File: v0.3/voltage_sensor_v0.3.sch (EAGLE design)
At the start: 56 parts, among them IC1 AP2112K-3.3TRG1, J2 236-404_000-009_999-950, J3 MC000048, J9 RJ11, T1 ZMPT101B, T2 ZMPT101B, T3 ZMPT101B

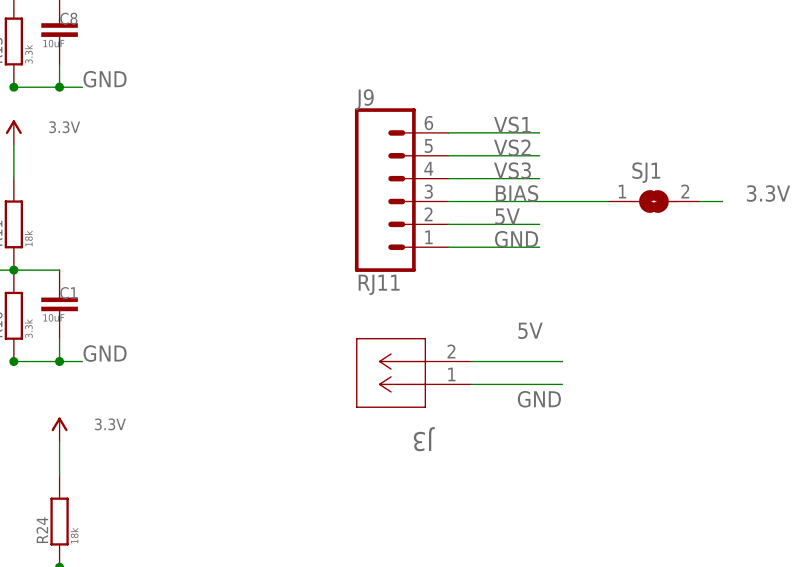
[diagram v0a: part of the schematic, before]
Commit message: rename change log
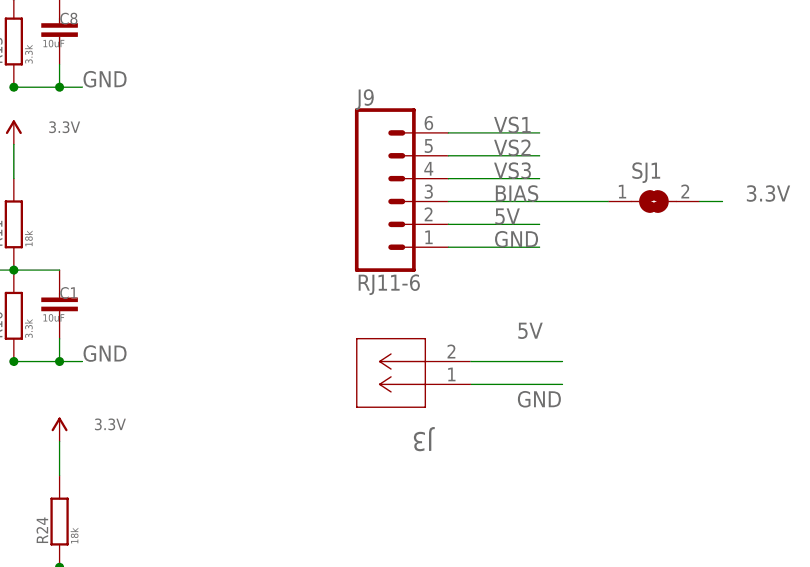
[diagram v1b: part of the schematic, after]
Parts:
- J9: value RJ11 -> RJ11-6
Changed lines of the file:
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@@
 <parts>
 <part name="T1" library="ZMPT101B" deviceset="ZMPT101B" device=""/>
-<part name="J9" library="SparkFun-Connectors" deviceset="RJ11-6" device="" value="RJ11"/>
+<part name="J9" library="SparkFun-Connectors" deviceset="RJ11-6" device="" value="RJ11-6"/>
 <part name="R22" library="rcl" deviceset="R-EU_" device="0204/7"/>
 <part name="R9" library="rcl" deviceset="R-EU_" device="R0603" value="75R"/>

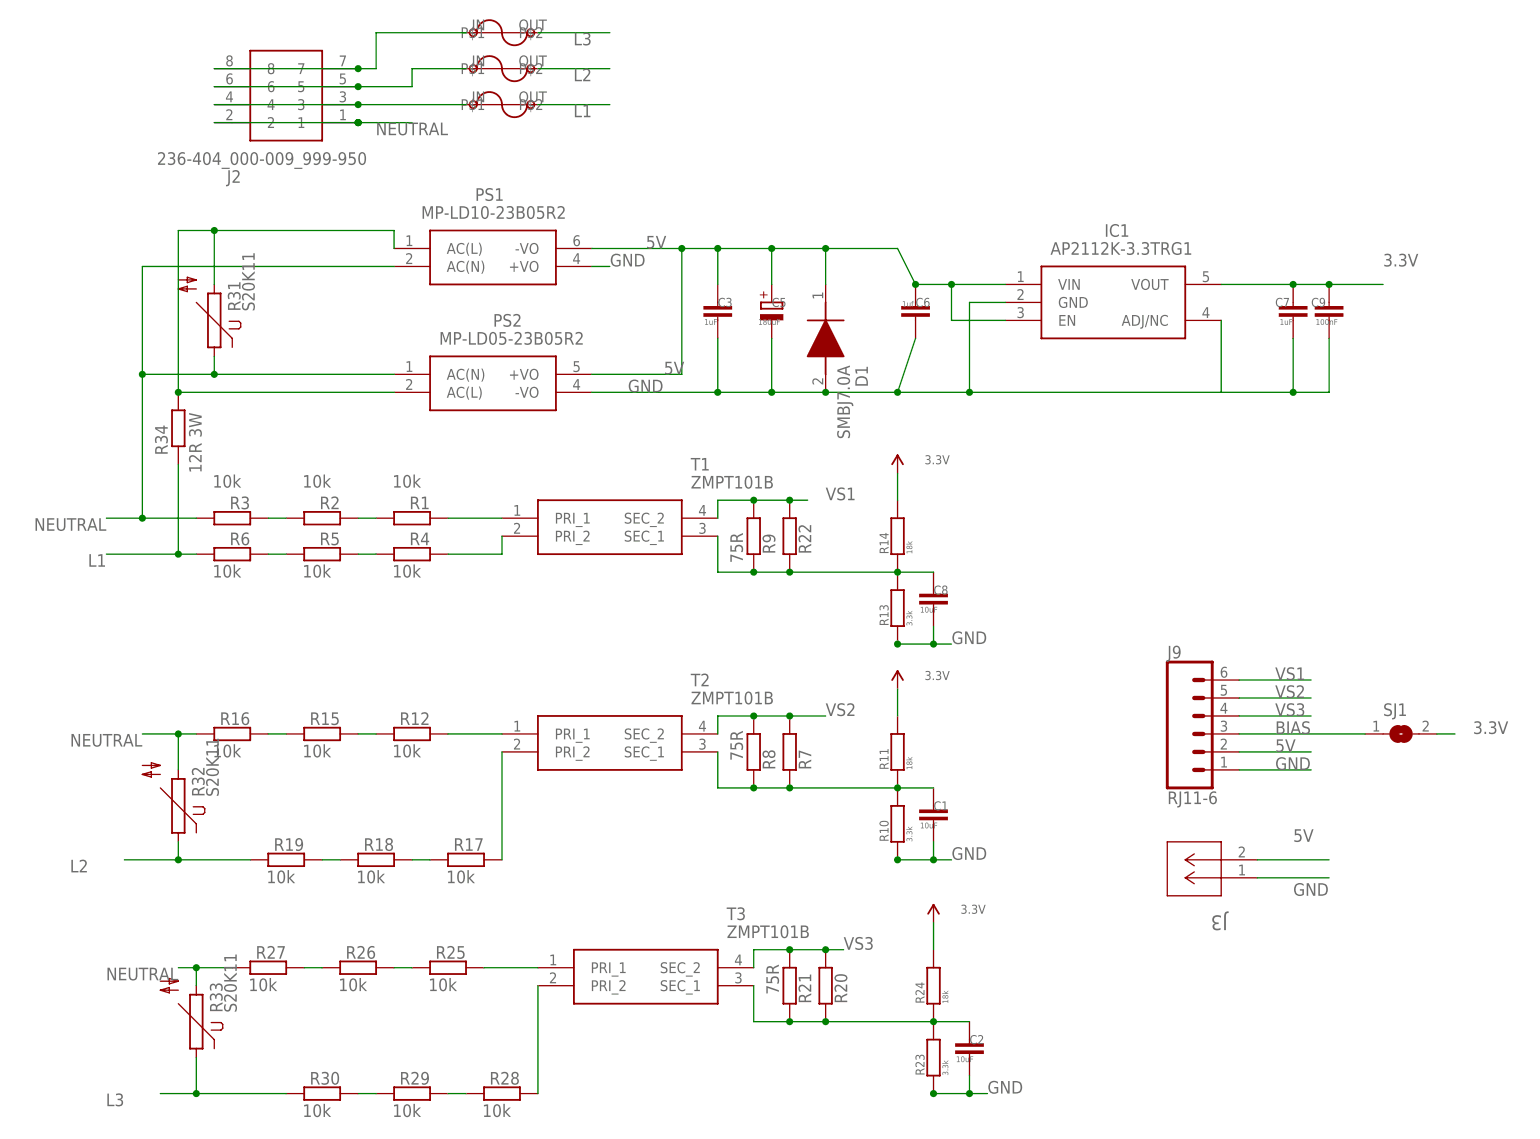
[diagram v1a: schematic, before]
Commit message: increase footprint of C5
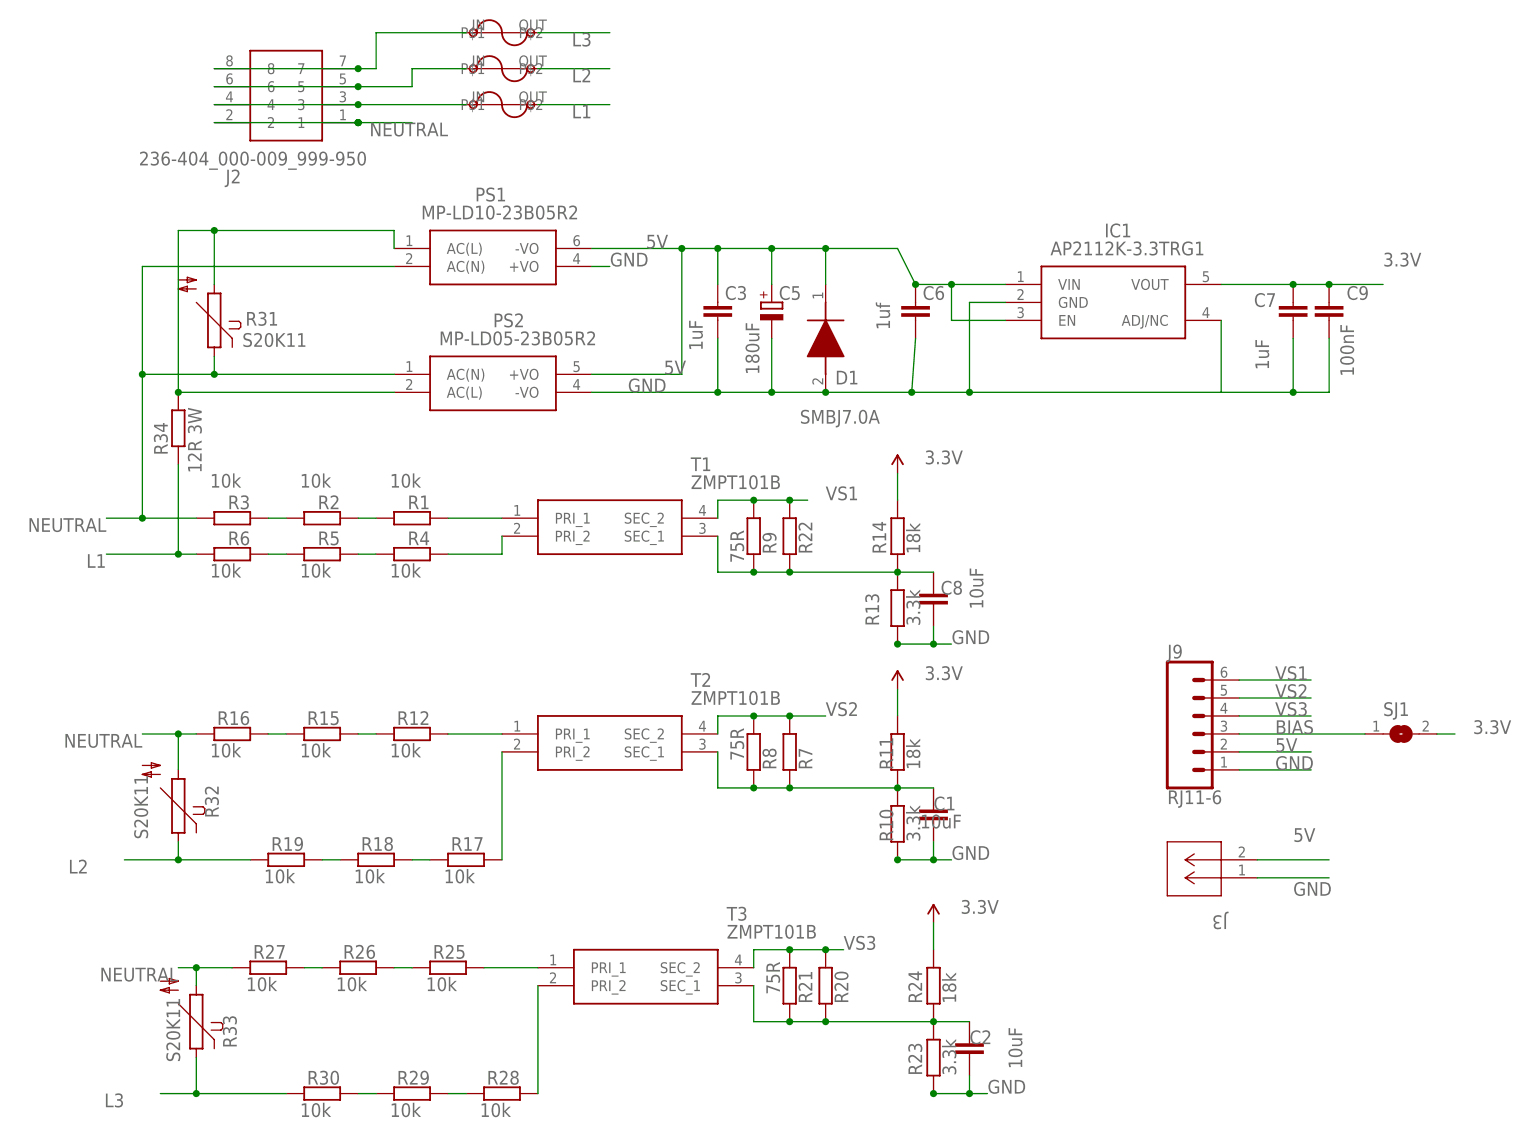
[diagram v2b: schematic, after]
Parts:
- C5: device rcl:CPOL-EUB -> rcl:CPOL-EUC

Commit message: v0.3 changes
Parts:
- removed J3: MC000048, 5mm-terminal:MC000048
- added J1: 1017505, 1017505:1017505
- J2: value 236-404_000-009_999-950 -> 20020316-H021B01LF; device 236-404_000-009_999-950:236-404_000-009_999-950 -> 20020316-H021B01LF:20020316-H021B01LF; ARROW_PART_NUMBER J2 -> (none)
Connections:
- net 5V: now also J2.2; no longer J3.2
- net GND: now also J2.1; no longer J3.1
- net L1: now also R31.1
- net N$16: now also J1.4.1, J1.4.2; no longer J2.7, J2.8
- net N$17: no longer R31.2
- net N$7: now also J1.2.1, J1.2.2; no longer J2.3, J2.4
- net N$8: now also J1.3.1, J1.3.2; no longer J2.5, J2.6
- net NEUTRAL: now also J1.1.1, J1.1.2, R31.2; no longer J2.1, J2.2, R31.1
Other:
- moved on the sheet: R31, R4, R5, R6
